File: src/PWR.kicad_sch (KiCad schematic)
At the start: 59 parts, among them J1 USB_C_Receptacle_USB2.0_16P, Q1 AO3401A, Q11 SI2308A, Q12 SI2308A, Q13 SI2308A, Q2 AO3401A, U14 TPS54302DDCR, U19 TPS54302DDCR, U4 TPS54302DDCR

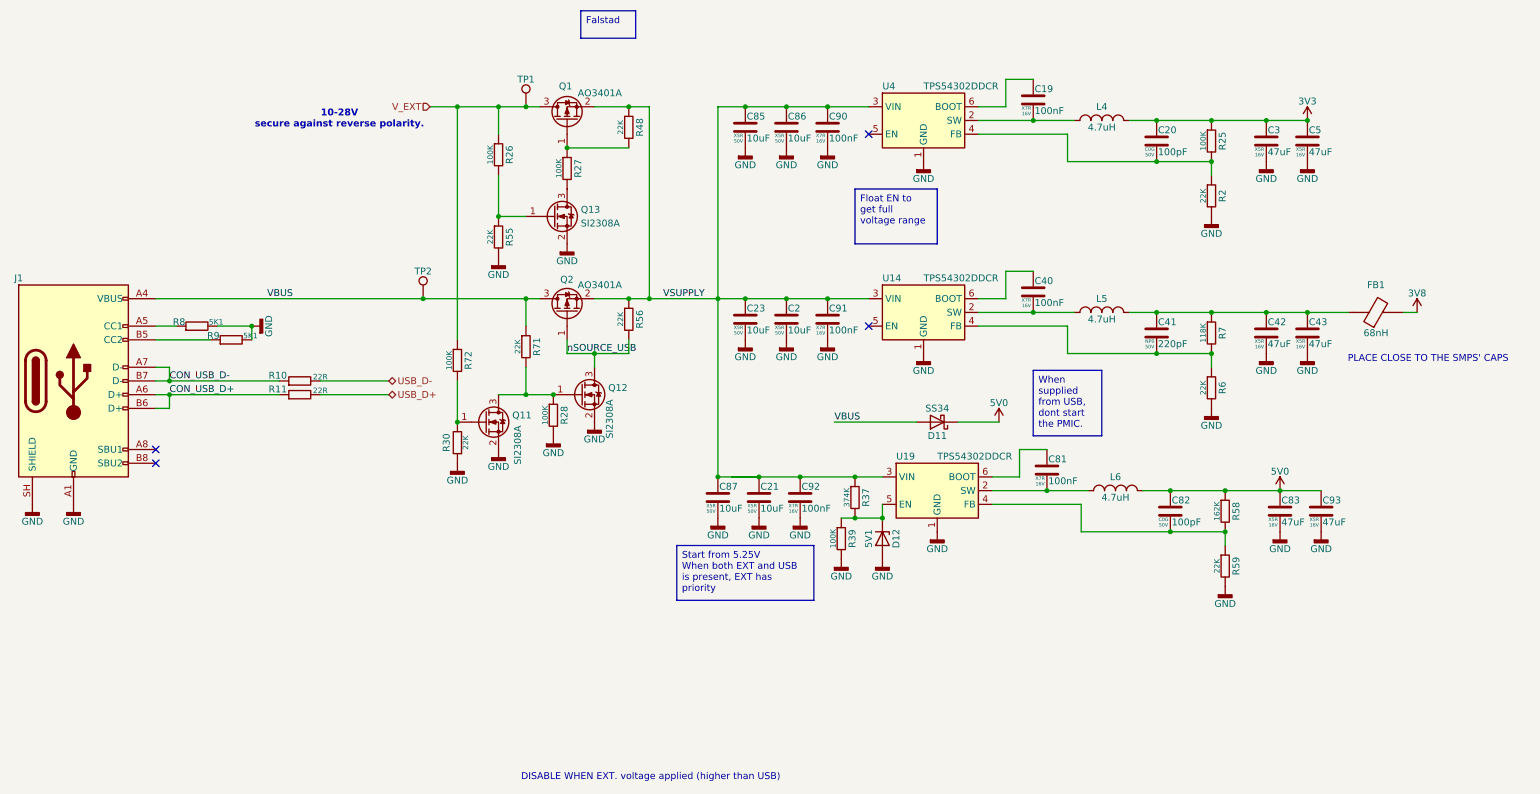
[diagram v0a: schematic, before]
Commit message: Update PCB layout and schematics; add enclosure design files
Bump firmware submodule to WAN failover scenario-audit hardening +
zombie-LTE self-heal (round 2).

Co-Authored-By: Claude Sonnet 5 <noreply@anthropic.com>
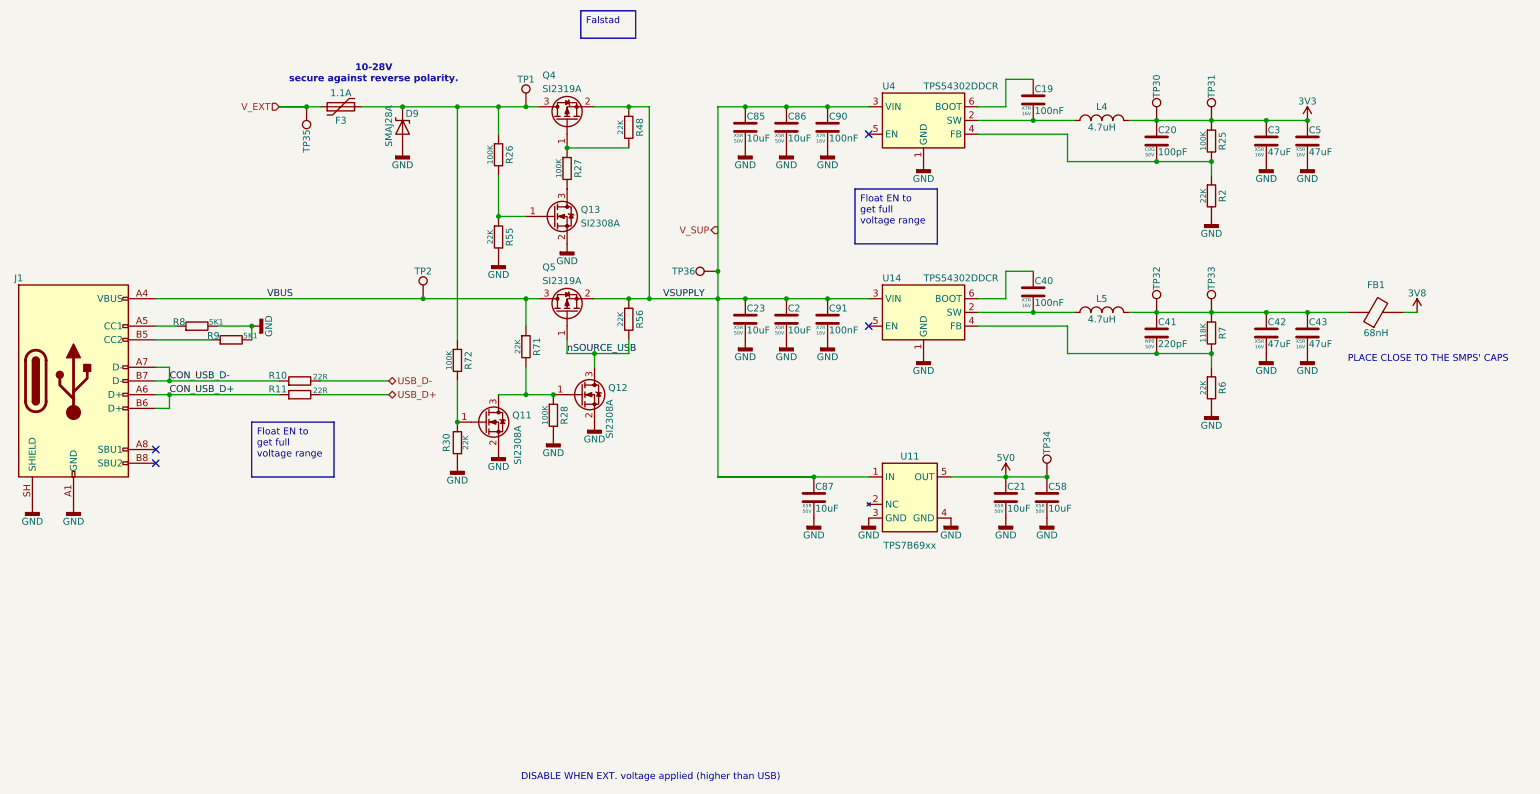
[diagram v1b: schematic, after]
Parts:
- removed C81, C92: 100nF, 7Sigma:C_0402_1005Metric, symbol Capacitor:CL05B104KO5NNNC
- removed C82: 100pF, 7Sigma:C_0402_1005Metric, symbol Capacitor:0402CG101J500NT
- removed C83, C93: 47uF, 7Sigma:C_1210_3225Metric, symbol Capacitor:CL32A476KOJNNNE
- removed D11: SS34, 7Sigma:D_SMA, symbol Diodes:SS34
- removed D12: 5V1, 7Sigma:D_SOD-123, symbol Diodes:BZT52C5V1
- removed L6: 4.7uH, 7Sigma:L_Changjiang_FTC404030S, symbol Inductors:FTC404030S4R7MGCA
- removed Q1, Q2: AO3401A, 7Sigma:SOT-23-3, symbol Transistors:AO3401A
- removed R37: 374K, 7Sigma:R_0402_1005Metric, symbol Resistor:0402WGF3743TCE
- removed R39: 100K, 7Sigma:R_0402_1005Metric, symbol Resistor:0402WGF1003TCE
- removed R58: 162K, 7Sigma:R_0402_1005Metric, symbol Resistor:0402WGF1623TCE
- removed R59: 22K, 7Sigma:R_0402_1005Metric, symbol Resistor:0402WGF2202TCE
- removed U19: TPS54302DDCR, 7Sigma:SOT-23-6, symbol ICs:TPS54302DDCR
- added C58: 10uF, 7Sigma:C_0805_2012Metric, symbol Capacitor:GRM21BR61H106KE43L
- added D9: SMAJ28A, 7Sigma:D_SMA, symbol Diodes:SMAJ28A
- added F3: 1.1A, 7Sigma:Fuse_1206_3216Metric, symbol Circuit_Protection:BSMD1206-110-30V
- added Q4, Q5: SI2319A, 7Sigma:SOT-23-3, symbol Transistors:SI2319A
- added TP30, TP31, TP32, TP33, TP34, TP35, TP36: TestPoint, 7Sigma:TestPoint_Pad_D1.5mm, symbol TestPoints:TestPoint_Pad_D1.5mm
- added U11: TPS7B69xx, 7Sigma:SOT-23-5, symbol ICs:TPS7B6950QDBVRQ1
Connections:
- net 3V3: now also TP30.1, TP31.1
- net 5V0: now also C21.1, C58.1, TP34.1, U11.5 (OUT)
- net GND: now also C58.2, D9.2 (A), U11.3 (GND), U11.4 (GND)
- net VBUS: now also Q5.3 (D)
- net V_EXT: now also F3.1, TP35.1; no longer R26.1, R72.1, TP1.1
- net nSOURCE_USB: now also Q5.1 (G)
- net at R27.1, R48.2: now also Q4.1 (G)
- net at C41.1, C42.1, C43.1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: now also TP32.1, TP33.1
- net VSUPPLY renamed V_SUP
- net V_SUP: now also Q4.2 (S), Q5.2 (S), TP36.1, U11.1 (IN); no longer C21.1
- new net: D9.1 (C), F3.2, Q4.3 (D), R26.1, R72.1, TP1.1
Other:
- moved on the sheet: C87
